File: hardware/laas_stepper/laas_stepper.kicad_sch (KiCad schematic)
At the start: 12 parts, among them J1 Conn_01x04_Pin, J2 Conn_01x04_Pin, J3 Conn_01x04_Pin, J4 Conn_01x02_Pin, U1 Pico

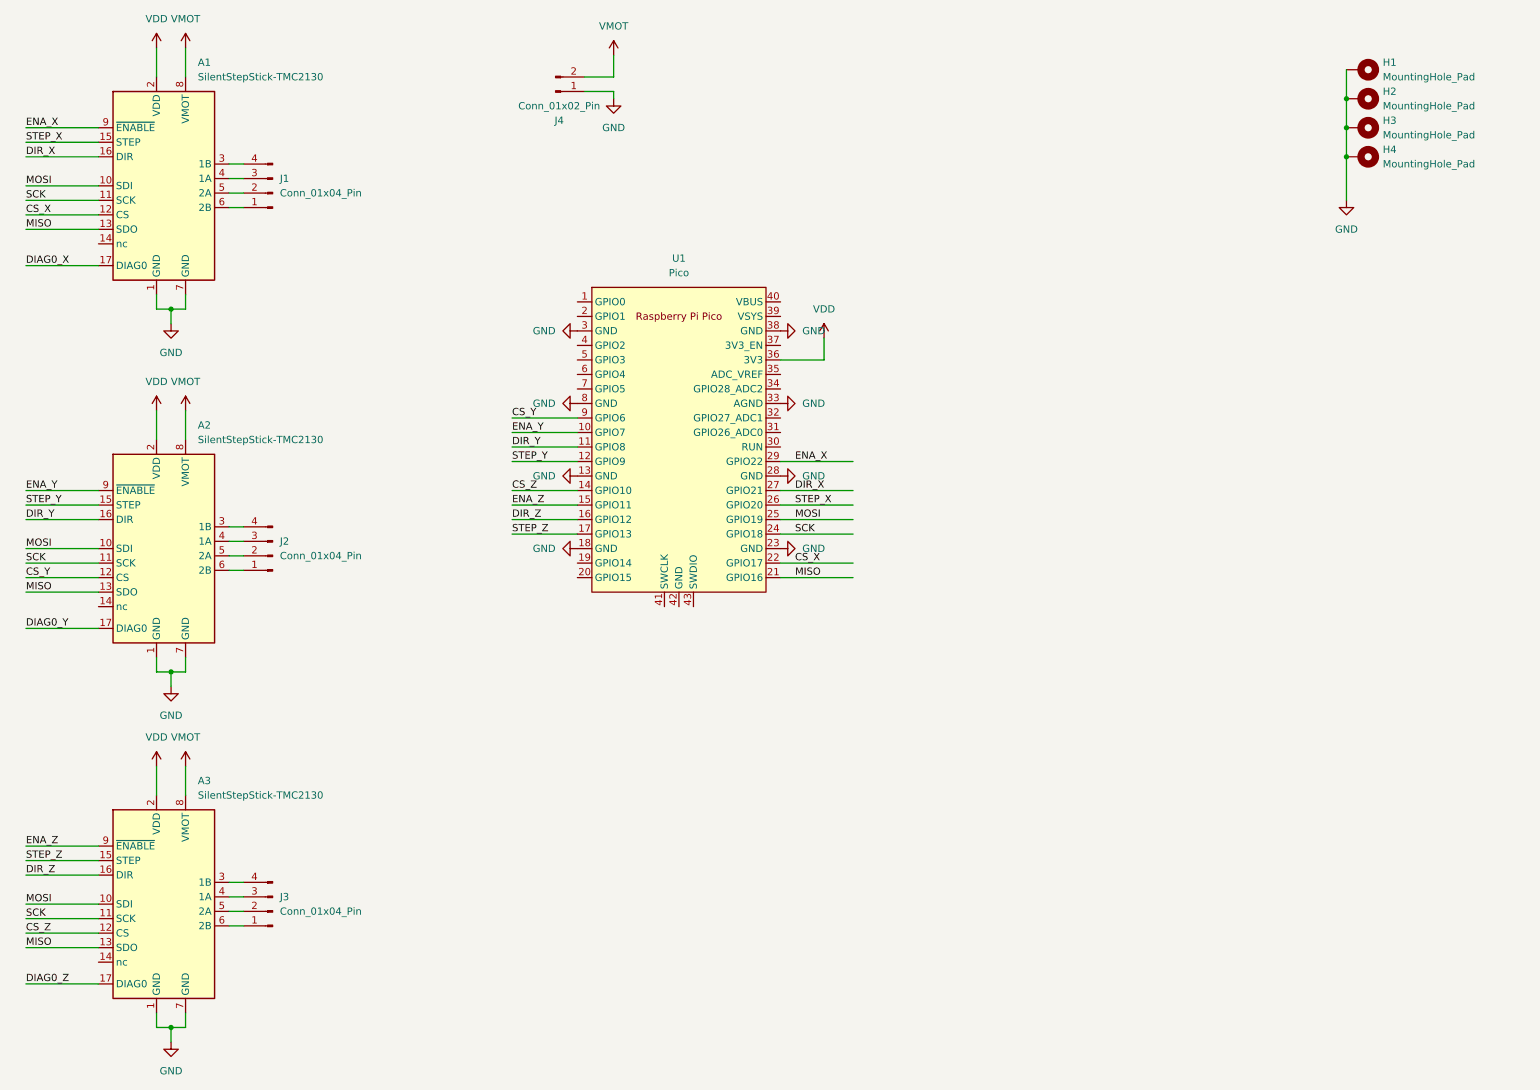
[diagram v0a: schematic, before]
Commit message: 4 axis version, with UV LED controller + GROVE connector; nex single axis with DC DC to make usb power optional, with GROVE connectors
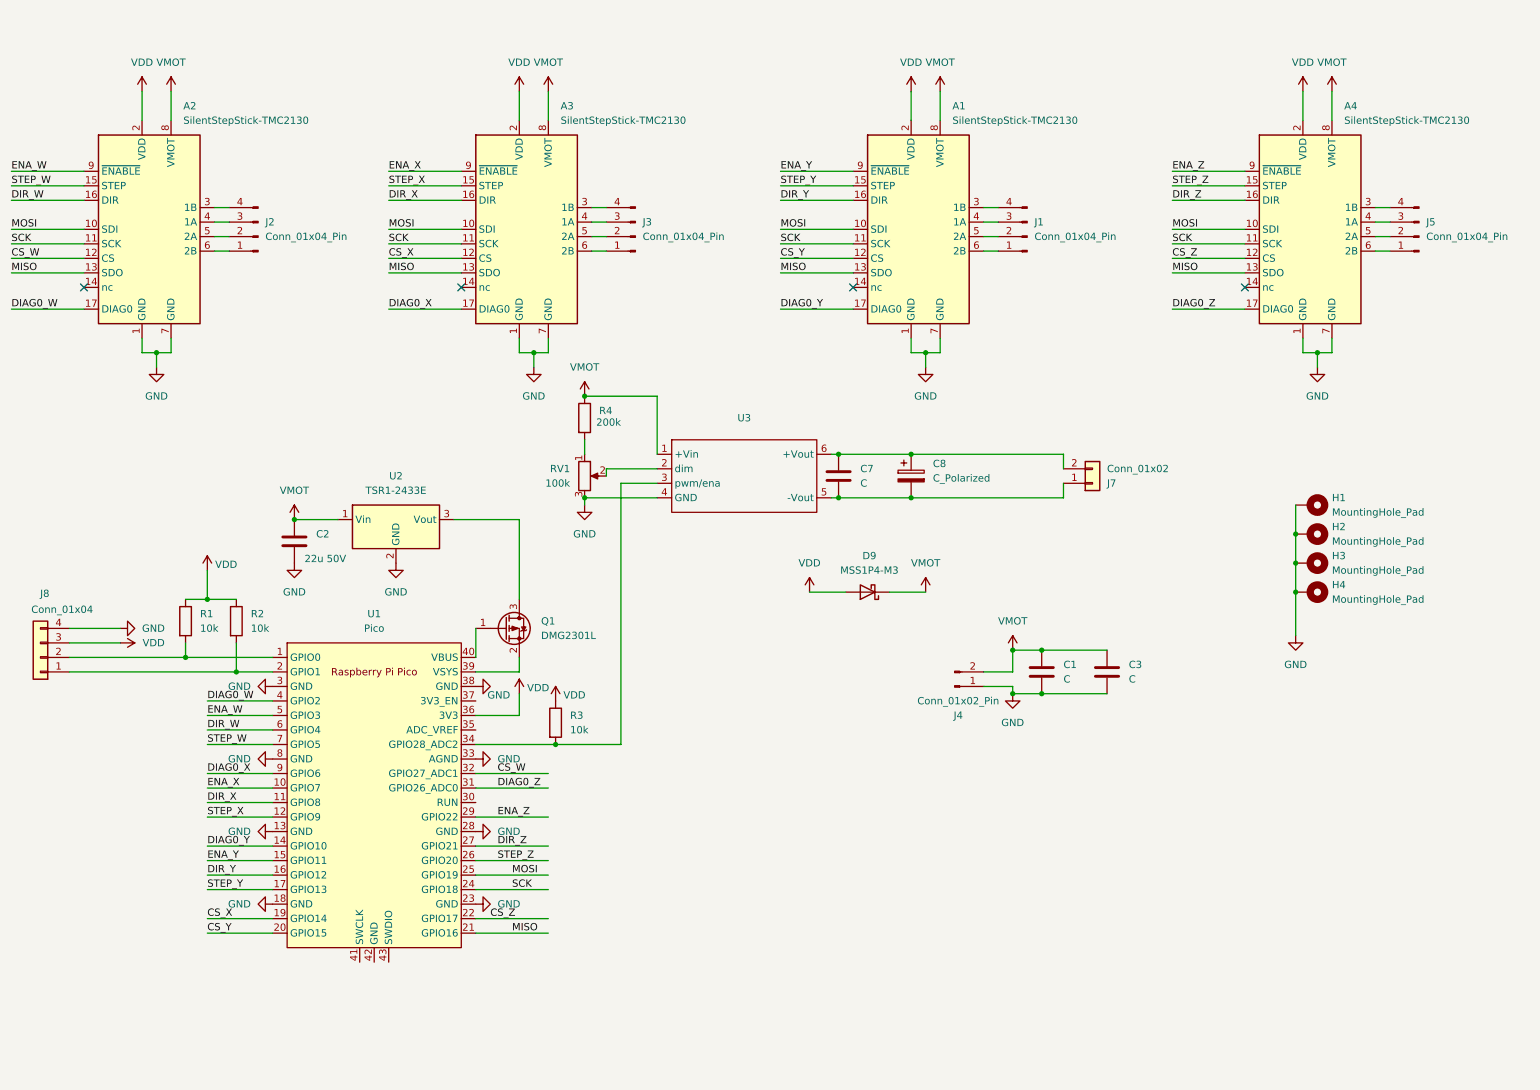
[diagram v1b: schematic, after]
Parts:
- added A4: SilentStepStick-TMC2130, TMC2301:Pololu_Breakout-16_15.2x20.3mm, symbol stepper_laas:Pololu_Breakout_A4988_1
- added C1, C3, C7: C, Capacitor_SMD:C_1210_3225Metric, symbol stepper_laas:C
- added C2: 22u 50V, Capacitor_SMD:C_1210_3225Metric, symbol stepper_laas:C
- added C8: C_Polarized, Capacitor_THT:CP_Radial_D8.0mm_P3.80mm, symbol Device:C_Polarized
- added D9: MSS1P4-M3, Diode_SMD:D_MicroSMP_AK, symbol stepper_laas:D_Schottky
- added J5: Conn_01x04_Pin, Connector_JST:JST_XA_B04B-XASK-1_1x04_P2.50mm_Vertical, symbol Connector:Conn_01x04_Pin
- added J7: Conn_01x02, Connector_JST:JST_XH_B2B-XH-A_1x02_P2.50mm_Vertical, symbol Connector_Generic:Conn_01x02
- added J8: Conn_01x04, Connector:NS-Tech_Grove_1x04_P2mm_Vertical, symbol Connector_Generic:Conn_01x04
- added Q1: DMG2301L, Package_TO_SOT_SMD:SOT-23, symbol Transistor_FET:DMG2301L
- added R1, R2, R3: 10k, Resistor_SMD:R_0805_2012Metric, symbol Device:R
- added R4: 200k, Resistor_SMD:R_0805_2012Metric, symbol Device:R
- added RV1: 100k, Potentiometer_THT:Potentiometer_Bourns_3296W_Vertical, symbol Device:R_Potentiometer
- added U2: TSR1-2433E, Converter_DCDC:Converter_DCDC_TRACO_TSR1-xxxxE_THT, symbol Regulator_Switching:TSR1-2433E
- added U3: ~, Library_custom:RCD-24_PL, symbol custom:RCD-24-PL
- A1, A2, A3: footprint Module:Pololu_Breakout-16_15.2x20.3mm -> TMC2301:Pololu_Breakout-16_15.2x20.3mm
- J1, J2, J3: footprint Connector_JST:JST_EH_B4B-EH-A_1x04_P2.50mm_Vertical -> Connector_JST:JST_XA_B04B-XASK-1_1x04_P2.50mm_Vertical
- U1: footprint MCU_RaspberryPi_and_Boards:RPi_Pico_SMD_TH -> Module:RaspberryPi_Pico_Common_Unspecified
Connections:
- net CS_X: now also A3.12 (CS), U1.19 (GPIO14); no longer A1.12 (CS), U1.22 (GPIO17)
- net CS_Y: now also A1.12 (CS), U1.20 (GPIO15); no longer A2.12 (CS), U1.9 (GPIO6)
- net CS_Z: now also U1.22 (GPIO17), A4.12 (CS); no longer A3.12 (CS), U1.14 (GPIO10)
- net DIAG0_X: now also A3.17 (DIAG0), U1.9 (GPIO6); no longer A1.17 (DIAG0)
- net DIAG0_Y: now also A1.17 (DIAG0), U1.14 (GPIO10); no longer A2.17 (DIAG0)
- net DIAG0_Z: now also U1.31 (GPIO26_ADC0), A4.17 (DIAG0); no longer A3.17 (DIAG0)
- net DIR_X: now also A3.16 (DIR), U1.11 (GPIO8); no longer A1.16 (DIR), U1.27 (GPIO21)
- net DIR_Y: now also A1.16 (DIR), U1.16 (GPIO12); no longer A2.16 (DIR), U1.11 (GPIO8)
- net DIR_Z: now also U1.27 (GPIO21), A4.16 (DIR); no longer A3.16 (DIR), U1.16 (GPIO12)
- net ENA_X: now also A3.9 (~{ENABLE}), U1.10 (GPIO7); no longer A1.9 (~{ENABLE}), U1.29 (GPIO22)
- net ENA_Y: now also A1.9 (~{ENABLE}), U1.15 (GPIO11); no longer A2.9 (~{ENABLE}), U1.10 (GPIO7)
- net ENA_Z: now also U1.29 (GPIO22), A4.9 (~{ENABLE}); no longer A3.9 (~{ENABLE}), U1.15 (GPIO11)
- net GND: now also A4.1 (GND), A4.7 (GND), C1.2, C2.2, C3.2, J8.4 (Pin_4), RV1.3, U2.2 (GND), U3.4 (GND)
- net MISO: now also A4.13 (SDO)
- net MOSI: now also A4.10 (SDI)
- net SCK: now also A4.11 (SCK)
- net STEP_X: now also A3.15 (STEP), U1.12 (GPIO9); no longer A1.15 (STEP), U1.26 (GPIO20)
- net STEP_Y: now also A1.15 (STEP), U1.17 (GPIO13); no longer A2.15 (STEP), U1.12 (GPIO9)
- net STEP_Z: now also U1.26 (GPIO20), A4.15 (STEP); no longer A3.15 (STEP), U1.17 (GPIO13)
- net VDD: now also A4.2 (VDD), D9.2 (A), J8.3 (Pin_3), R1.1, R2.1, R3.1
- net VMOT: now also A4.8 (VMOT), C1.1, C2.1, C3.1, D9.1 (K), R4.1, U2.1 (Vin), U3.1 (+Vin)
- net at U1.1 (GPIO0): now also J8.2 (Pin_2), R1.2
- net at U1.2 (GPIO1): now also J8.1 (Pin_1), R2.2
- net CS_W: now reaches U1.32 (GPIO27_ADC1)
- net CS_W: now also A2.12 (CS)
- net at U1.34 (GPIO28_ADC2): now also R3.2, U3.3 (pwm/ena)
- net at U1.39 (VSYS): now also Q1.2 (S)
- net DIAG0_W: now reaches U1.4 (GPIO2)
- net DIAG0_W: now also A2.17 (DIAG0)
- net at U1.40 (VBUS): now also Q1.1 (G)
- net ENA_W: now reaches U1.5 (GPIO3)
- net ENA_W: now also A2.9 (~{ENABLE})
- net DIR_W: now reaches U1.6 (GPIO4)
- net DIR_W: now also A2.16 (DIR)
- net STEP_W: now reaches U1.7 (GPIO5)
- net STEP_W: now also A2.15 (STEP)
- new net: A4.6 (2B), J5.1 (Pin_1)
- new net: A4.5 (2A), J5.2 (Pin_2)
- new net: A4.4 (1A), J5.3 (Pin_3)
- new net: A4.3 (1B), J5.4 (Pin_4)
- new net: R4.2, RV1.1
- new net: RV1.2, U3.2 (dim)
- new net: C7.1, C8.1, J7.2 (Pin_2), U3.6 (+Vout)
- new net: C7.2, C8.2, J7.1 (Pin_1), U3.5 (-Vout)
- new net: Q1.3 (D), U2.3 (Vout)
- no-connect marks 0 -> 4
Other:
- moved on the sheet: A1, A2, A3, H1, H2, H3, H4, J1, J2, J3, J4, U1

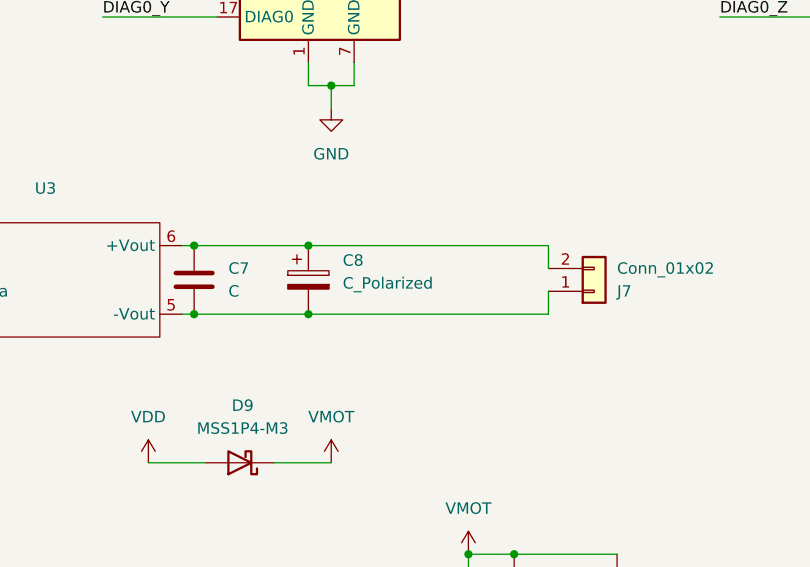
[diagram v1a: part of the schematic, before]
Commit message: Adapt firmware to custom board.
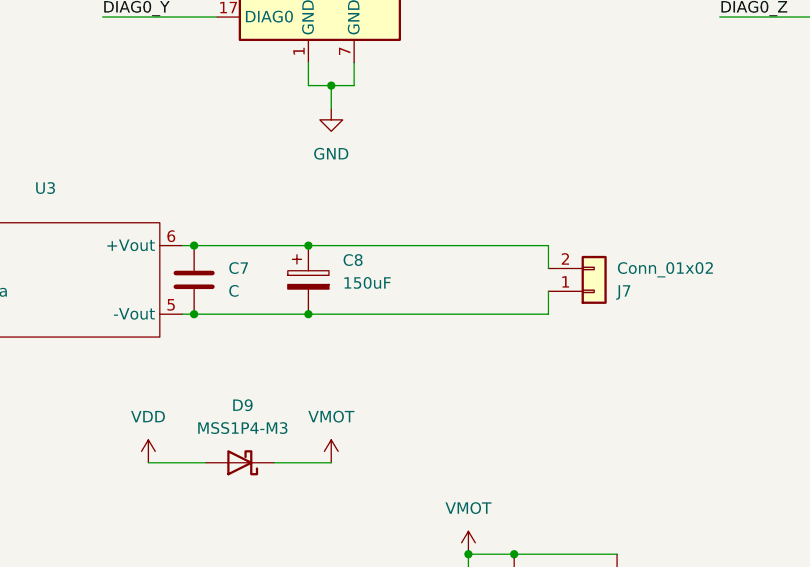
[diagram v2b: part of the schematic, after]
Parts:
- C8: value C_Polarized -> 150uF; ref (none) -> 35ZLG150MEFC8X11.5
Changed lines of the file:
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@@
 			)
 		)
-		(property "Value" "C_Polarized"
+		(property "Value" "150uF"
 			(at 179.07 95.6309 0)
 			(effects
@@
 			(at 175.26 95.25 0)
 			(effects
+				(font
+					(size 1.27 1.27)
+				)
+				(hide yes)
+			)
+		)
+		(property "ref" "35ZLG150MEFC8X11.5"
+			(at 175.26 95.25 0)
+			(effects
